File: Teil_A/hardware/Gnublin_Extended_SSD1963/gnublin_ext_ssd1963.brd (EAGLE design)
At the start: 81.2 x 72.4 mm, 8 parts

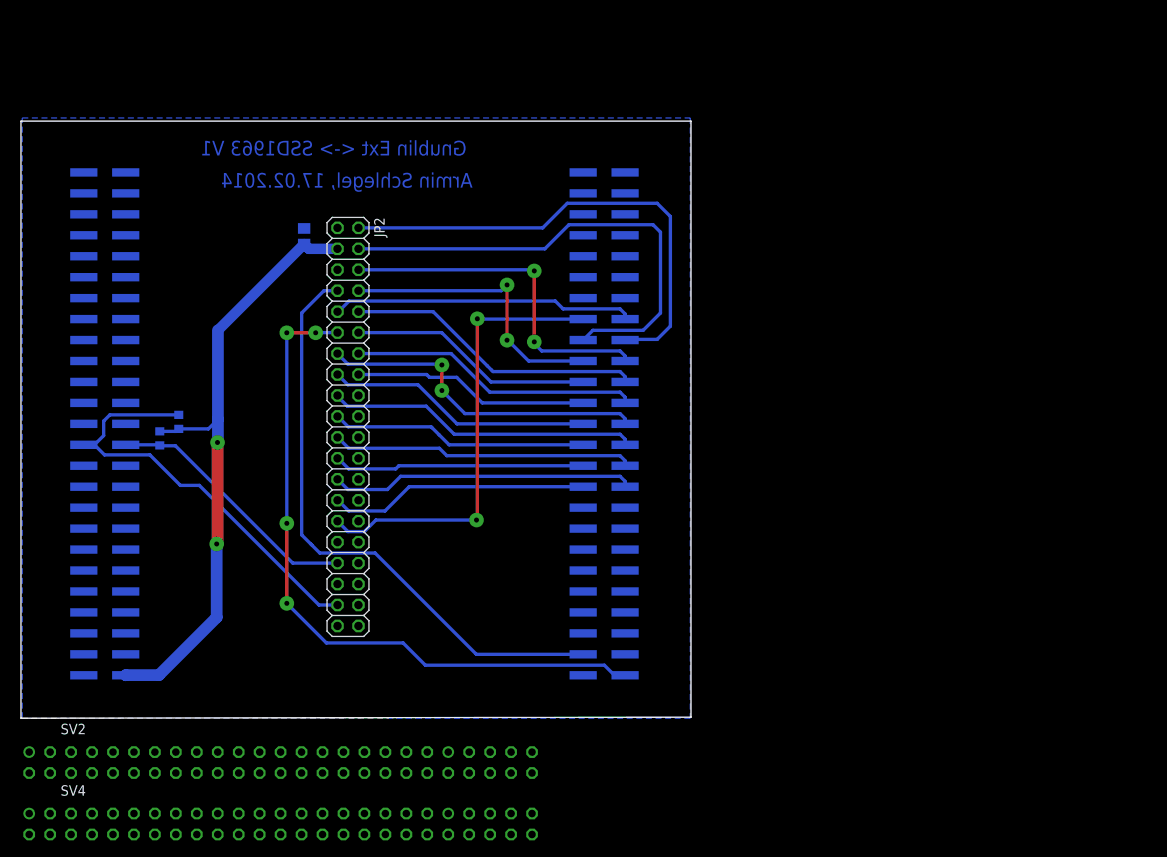
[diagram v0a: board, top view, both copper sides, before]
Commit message: updated TEIL_A schematics and layout; git commit -am 'updated TEIL_A schematics and layout
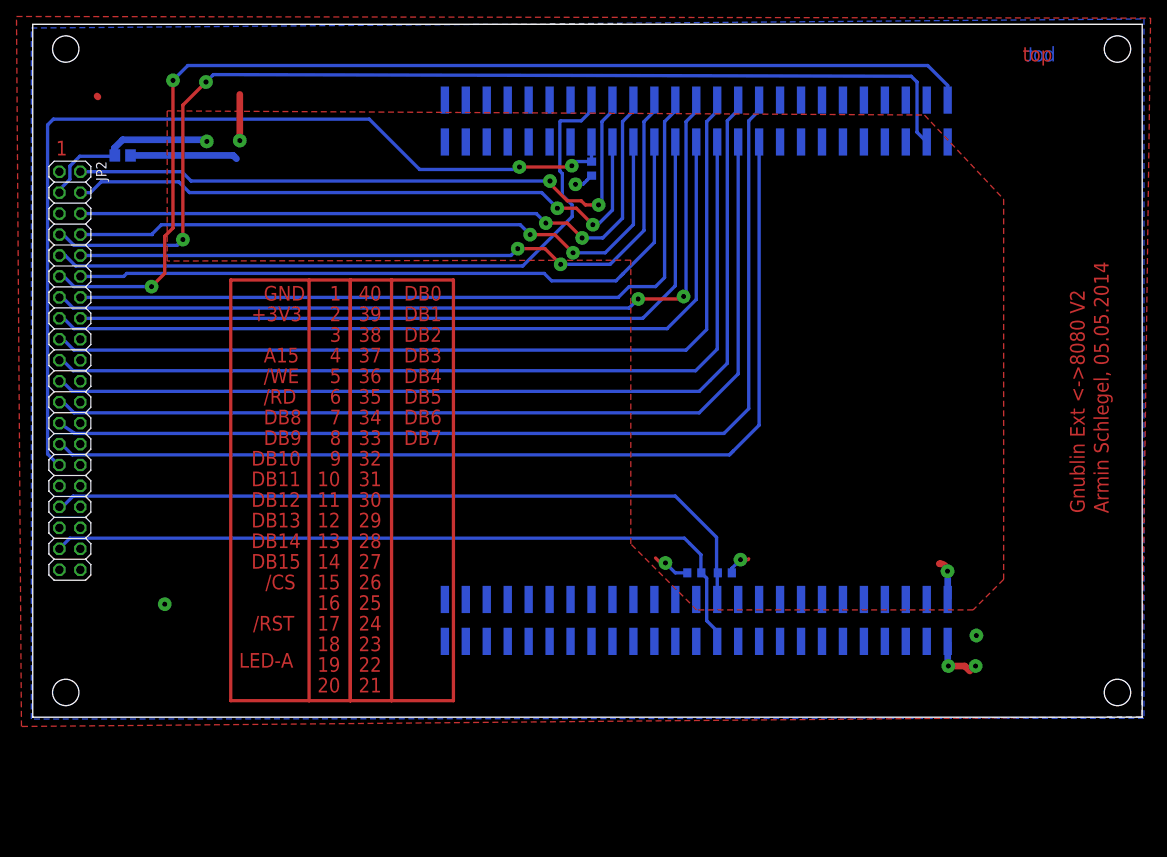
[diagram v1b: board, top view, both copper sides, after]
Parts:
- removed SV2, SV4: (no value), con-lsta:FE25-2
- added R3: 10k, rcl:R0603
- moved JP3 99.9 mm to (109.7, 13.0), turned to 0 degrees
- moved R1 70.4 mm to (83.9, 17.5), turned to 180 degrees
- moved R2 65.1 mm to (80.2, 17.5), turned to 0 degrees
- moved JP2 34.4 mm to (4.50, 42.0)
- moved C1 24.1 mm to (10.9, 68.1), turned to 180 degrees
- moved JP1 17.9 mm to (51.2, 71.0), turned to 180 degrees
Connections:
- removed net +5V: SV2.4, SV4.3
- removed net CTS_N: SV2.25
- removed net GPIO0: SV2.3
- removed net GPIO1: SV2.6
- removed net GPIO11: SV2.16
- removed net GPIO12: SV2.15
- removed net GPIO13: SV2.18
- removed net GPIO14: SV2.17
- removed net GPIO15: SV2.20
- removed net GPIO16: SV2.19
- removed net GPIO17: SV2.22
- removed net GPIO18: SV2.21
- removed net GPIO2: SV2.5
- removed net GPIO3: SV2.8
- removed net GPIO4: SV2.7
- removed net I2C_SCL0: SV2.32
- removed net I2C_SCL1: SV2.31
- removed net I2C_SDA0: SV2.34
- removed net I2C_SDA1: SV2.33
- removed net I2SRX_BCK0: SV2.43
- removed net I2SRX_BCK1: SV2.44
- removed net I2SRX_D0: SV2.47
- removed net I2SRX_D1: SV2.48
- removed net I2SRX_WS0: SV2.45
- removed net I2SRX_WS1: SV2.46
- removed net I2STX_BCK0: SV2.37
- removed net I2STX_BCK1: SV2.38
- removed net I2STX_CLK0: SV2.35
- removed net I2STX_D0: SV2.41
- removed net I2STX_D1: SV2.42
- removed net I2STX_WS0: SV2.39
- removed net I2STX_WS1: SV2.40
- removed net LPC_A0: SV4.33
- removed net LPC_A1: SV4.34
- removed net LPC_A10: SV4.43
- removed net LPC_A11: SV4.44
- removed net LPC_A12: SV4.45
- removed net LPC_A13: SV4.46
- removed net LPC_A14: SV4.47
- removed net LPC_A2: SV4.35
- removed net LPC_A3: SV4.36
- removed net LPC_A4: SV4.37
- removed net LPC_A5: SV4.38
- removed net LPC_A6: SV4.39
- removed net LPC_A7: SV4.40
- removed net LPC_A8: SV4.41
- removed net LPC_A9: SV4.42
- removed net LPC_CKE: SV4.13
- removed net LPC_CS: SV4.14
- removed net LPC_D0: SV4.17
- removed net LPC_D1: SV4.18
- removed net LPC_D10: SV4.27
- removed net LPC_D11: SV4.28
- removed net LPC_D12: SV4.29
- removed net LPC_D13: SV4.30
- removed net LPC_D14: SV4.31
- removed net LPC_D15: SV4.32
- removed net LPC_D2: SV4.19
- removed net LPC_D3: SV4.20
- removed net LPC_D4: SV4.21
- removed net LPC_D5: SV4.22
- removed net LPC_D6: SV4.23
- removed net LPC_D7: SV4.24
- removed net LPC_D8: SV4.25
- removed net LPC_D9: SV4.26
- removed net LPC_DQM1: SV4.12
- removed net LPC_MCI_CD: SV4.10
- removed net LPC_MCI_CLK: SV2.10
- removed net LPC_MCI_CMD: SV2.9
- removed net LPC_MCI_DAT0: SV2.12
- removed net LPC_MCI_DAT1: SV2.11
- removed net LPC_MCI_DAT2: SV2.14
- removed net LPC_MCI_DAT3: SV2.13
- removed net NCS0: SV4.4
- removed net NCS1: SV4.5
- removed net NCS2: SV4.6
- removed net NCS3: SV4.7
- removed net RTS_N: SV2.28
- removed net RXD: SV2.30
- removed net RYBN0: SV4.8
- removed net RYBN1: SV4.9
- removed net RYBN3: SV4.11
- removed net TXD: SV2.27
- net +3V3: now also R3.2; no longer SV2.2, SV2.49, SV4.1, SV4.50
- net GND: no longer SV2.1, SV2.26, SV2.29, SV2.36, SV2.50, SV4.2
- net GPIO19: no longer SV2.24
- net GPIO20: no longer SV2.23
- net LPC_A15: no longer SV4.48
- net LPC_DQM0: no longer SV4.49
- net LPC_WE: no longer SV4.15
- net STCS0: now also R3.1; no longer SV4.16
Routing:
- net N$1: track 0.00 -> 182.0 mm
- net N$2: track 0.00 -> 178.0 mm
- net LPC_DB15: track 31.5 -> 121.7 mm
- net LPC_DB14: track 36.9 -> 123.1 mm
- net LPC_DB13: track 30.5 -> 112.9 mm
- net LPC_DB12: track 36.6 -> 115.3 mm
- net LPC_DB11: track 31.2 -> 106.4 mm
- net LPC_DB10: track 37.8 -> 108.4 mm
- net LPC_DB9: track 32.3 -> 98.3 mm
- net LPC_DB7: track 28.7 -> 91.2 mm
- net LPC_DB8: track 40.6 -> 101.2 mm
- net LPC_DB6: track 35.2 -> 93.9 mm
- net GPIO19: track 31.6 -> 89.9 mm
- net STCS0: track 55.2 -> 113.4 mm
- net LPC_A15: track 72.5 -> 130.7 mm, vias 0 -> 2
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- added copper zone on layer 1, net +3V3
- added copper zone on layer 1, net GND
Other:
- board size 81.2 x 72.4 mm -> 134.5 x 84 mm
- board text added: "+3V3"
- board text added: "/CS"
- board text added: "/RD"
- board text added: "/RST"
- board text added: "/WE"
- board text added: "1"
- board text added: "10"
- board text added: "11"
- board text added: "12"
- board text added: "13"
- board text added: "14"
- board text added: "15"
- board text added: "16"
- board text added: "17"
- board text added: "18"
- board text added: "19"
- board text added: "2"
- board text added: "20"
- board text added: "21"
- board text added: "22"
- board text added: "23"
- board text added: "24"
- board text added: "25"
- board text added: "26"
- board text added: "27"
- board text added: "28"
- board text added: "29"
- board text added: "3"
- board text added: "30"
- board text added: "31"
- board text added: "32"
- board text added: "33"
- board text added: "34"
- board text added: "35"
- board text added: "36"
- board text added: "37"
- board text added: "38"
- board text added: "39"
- board text added: "4"
- board text added: "40"
- board text added: "5"
- board text added: "6"
- board text added: "7"
- board text added: "8"
- board text added: "9"
- board text added: "A15"
- board text added: "Armin Schlegel, 05.05.2014"
- board text added: "DB0"
- board text added: "DB1"
- board text added: "DB10"
- board text added: "DB11"
- board text added: "DB12"
- board text added: "DB13"
- board text added: "DB14"
- board text added: "DB15"
- board text added: "DB2"
- board text added: "DB3"
- board text added: "DB4"
- board text added: "DB5"
- board text added: "DB6"
- board text added: "DB7"
- board text added: "DB8"
- board text added: "DB9"
- board text added: "GND"
- board text added: "Gnublin Ext <->8080 V2"
- board text added: "LED-A"
- board text added: "bot"
- board text added: "top"
- board text removed: "Armin Schlegel, 17.02.2014"
- board text removed: "Gnublin Ext <-> SSD1963 V1"
